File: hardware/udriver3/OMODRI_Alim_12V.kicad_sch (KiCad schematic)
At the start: 13 parts, among them U15 MP4572GQB

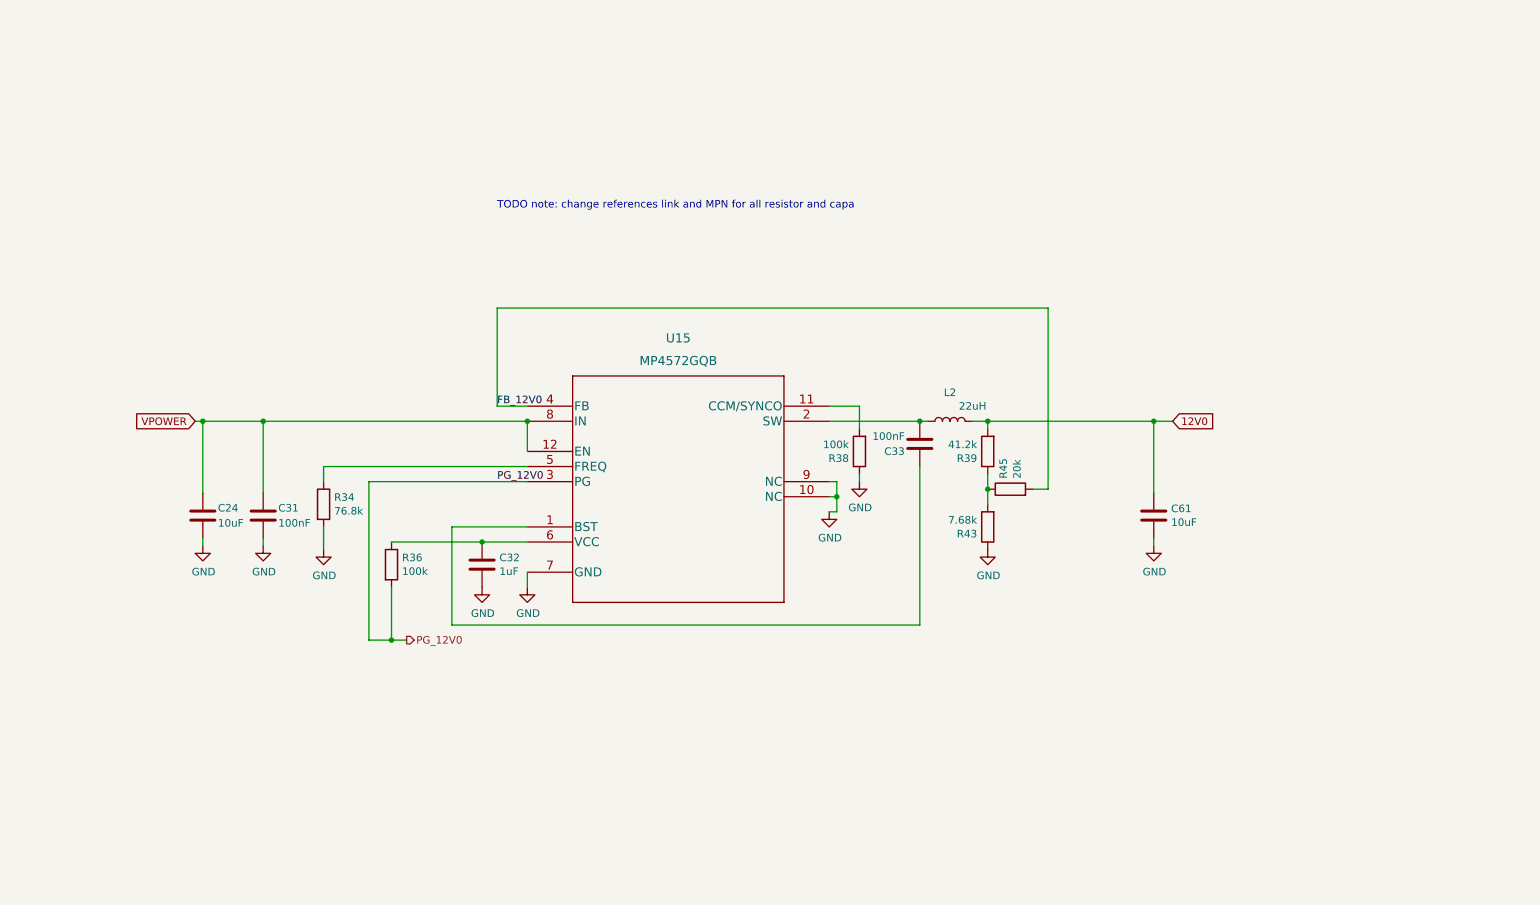
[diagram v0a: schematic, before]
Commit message: Schematics update. 12V0 and 5V0 power supplies not finished yet. RS485 added but not connected to F28388 mcu.
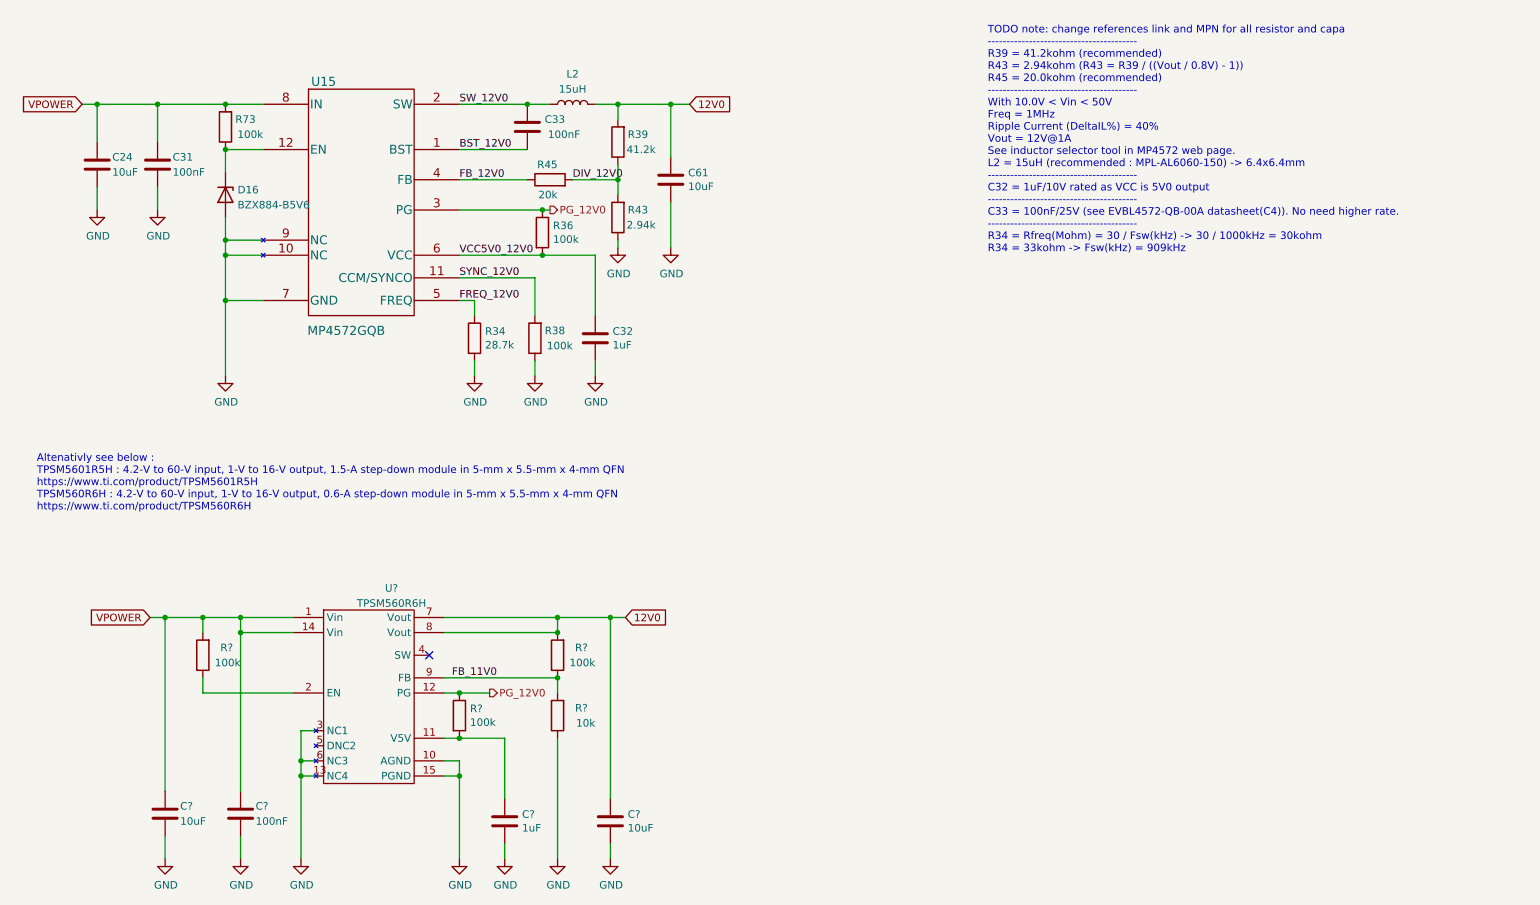
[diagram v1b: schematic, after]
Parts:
- added C?: 100nF, Capacitor_SMD:C_0603_1608Metric, symbol Device:C
- added C?: 10uF, Capacitor_SMD:C_1210_3225Metric, symbol Device:C
- added C?: 10uF, Capacitor_SMD:C_0603_1608Metric, symbol Device:C
- added C?: 1uF, Capacitor_SMD:C_0201_0603Metric, symbol Device:C
- added D16: BZX884-B5V6, udriver3:DFN1006-2, symbol Device:D_Zener
- added R73, R?: 100k, Resistor_SMD:R_0402_1005Metric, symbol Device:R
- added R? (x2): 100k, Resistor_SMD:R_0201_0603Metric, symbol Device:R
- added R?: 10k, Resistor_SMD:R_0201_0603Metric, symbol Device:R
- added U?: TPSM560R6H, symbol omodri_lib:TPSM560R6H
- C33: footprint Capacitor_SMD:C_0603_1608Metric -> Capacitor_SMD:C_0201_0603Metric; DigiKey 490-3285-1-ND -> 490-14571-1-ND; Farnell 1828921 -> 3790414; Mouser 81-GRM188R72A104KA35 -> 81-GRM033R61E104KE4J; Part No GRM188R72A104KA35D -> GRM033R61E104KE14J; RS (none) -> 185-2066; Rated Voltage 100V -> 25V
- C61: DigiKey 490-10475-1-ND -> 490-7202-2-ND; Farnell 2456110 -> 2695906; Mouser 81-GRM188R61A106ME9D -> 81-GRM188R61E106MA3D; Part No GRM188R61A106ME69D -> GRM188R61E106MA73D; RS 113-8702 -> 815-1377; Rated Voltage 10V -> 25V
- L2: value 22uH -> 15uH
- R34: value 76.8k -> 28.7k
- R43: value 7.68k -> 2.94k
- U15: footprint udriver3:MP4572GQB -> udriver3:QFN-12_2.5x3mm_P0.5mm_MPS; DigiKey (none) -> 1589-MP4572GQB-PTR-ND; Farnell (none) -> 3935113; Mouser (none) -> 946-MP4572GQB-P; Part No (none) -> MP4572GQB-P
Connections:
- net 12V0: now also C?.1, R?.2, U?.7 (Vout), U?.8 (Vout)
- net FB_12V0: now also R45.1; no longer R45.2
- net GND: now also C?.2, C?.2, C?.2, C?.2, D16.2 (A), R?.1, U?.10 (AGND), U?.13 (NC4), U?.15 (PGND), U?.3 (NC1), U?.6 (NC3)
- net PG_12V0: now also R36.1, R?.1, U?.12 (PG); no longer R36.2
- net VPOWER: now also C?.1, C?.1, R73.2, R?.2, U?.1 (Vin), U?.14 (Vin); no longer U15.12 (EN)
- net BST_12V0: now reaches C33.1, U15.1 (BST)
- net SYNC_12V0: now reaches R38.2, U15.11 (CCM/SYNCO)
- net SW_12V0: now reaches C33.2, L2.1, U15.2 (SW)
- net FREQ_12V0: now reaches R34.1, U15.5 (FREQ)
- net VCC5V0_12V0: now reaches C32.1, U15.6 (VCC)
- net VCC5V0_12V0: now also R36.2; no longer R36.1
- net DIV_12V0: now reaches R39.1, R43.2
- net DIV_12V0: now also R45.2; no longer R45.1
- new net: D16.1 (K), R73.1, U15.12 (EN)
- new net: C?.1, R?.2, U?.11 (V5V)
- new net: R?.1, U?.2 (EN)
- new net FB_11V0: R?.1, R?.2, U?.9 (FB)
- no-connect marks 0 -> 1
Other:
- note added: "Altenativly see below : TPSM5601R5H : 4.2-V to 60-V input, 1-V to 16-V output, 1.5-A step-down module in 5-mm x 5.5-mm x 4-mm QFN https://www.ti.com/product/TPSM5601R5H TPSM560R6H : 4.2-V to 60-V input, 1-V to 16-V output, 0.6-A step-down module in 5-mm x 5.5-mm x 4-mm QFN https://www.ti.com/product/TPSM560R6H"
- note added: "TODO note: change references link and MPN for all resistor and capa ---------------------------------------- R39 = 41.2kohm (recommended) R43 = 2.94kohm (R43 = R39 / ((Vout / 0.8V) - 1)) R45 = 20.0kohm (recommended) ---------------------------------------- With 10.0V < Vin < 50V Freq = 1MHz Ripple Current (DeltaIL%) = 40% Vout = 12V@1A See inductor selector tool in MP4572 web page. L2 = 15uH (rec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"
- note removed: "TODO note: change references link and MPN for all resistor and capa"
- company: (none) -> LAAS/CNRS
- title: (none) -> Open MOtor DRiver Initiative (OMODRI)
- moved on the sheet: C24, C31, C32, C33, C61, L2, R34, R36, R39, R43, R45

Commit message: Temporary version of udrive3 v2.0. - In schematic there are 2 solutions for DC/DC buck converter. - PCB routing is not finished yet.
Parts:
- removed R?: 100k, Resistor_SMD:R_0402_1005Metric, symbol Device:R
- R53: renamed from R?; DigiKey (none) -> P122655CT-ND; Farnell (none) -> 2302389; Mouser (none) -> 667-ERJ-1GNF1003C; Part No (none) -> ERJ-1GNF1003C; RS (none) -> 179-7130; Rated Voltage (none) -> Resistor_SMD:R_0201_0603Metric
- R59: renamed from R?; DigiKey (none) -> P122414CT-ND; Farnell (none) -> 2302362; Mouser (none) -> 667-ERJ-1GNF1002C; Part No (none) -> ERJ-1GNF1002C; RS (none) -> 176-3597
- U16: renamed from U?; footprint (none) -> udriver3:B3QFN_15; DigiKey (none) -> 296-TPSM560R6HRDARTR-ND; Mouser (none) -> 595-TPSM560R6HRDAR; Part No (none) -> TPSM560R6HRDAR
- gave numbers to parts that had none: 5
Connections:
- net 12V0: no longer C89.1, R53.2, U16.7 (Vout), U16.8 (Vout)
- net PG_12V0: no longer R57.1, U16.12 (PG)
- net VPOWER: now also U16.2 (EN)
- net EN_12V0: now reaches D16.1 (K), R73.1, U15.12 (EN)
- new net 12V0_1: C89.1, R53.2, U16.7 (Vout), U16.8 (Vout)
- new net PG_12V0_1: R57.1, U16.12 (PG)
- no-connect marks 1 -> 0

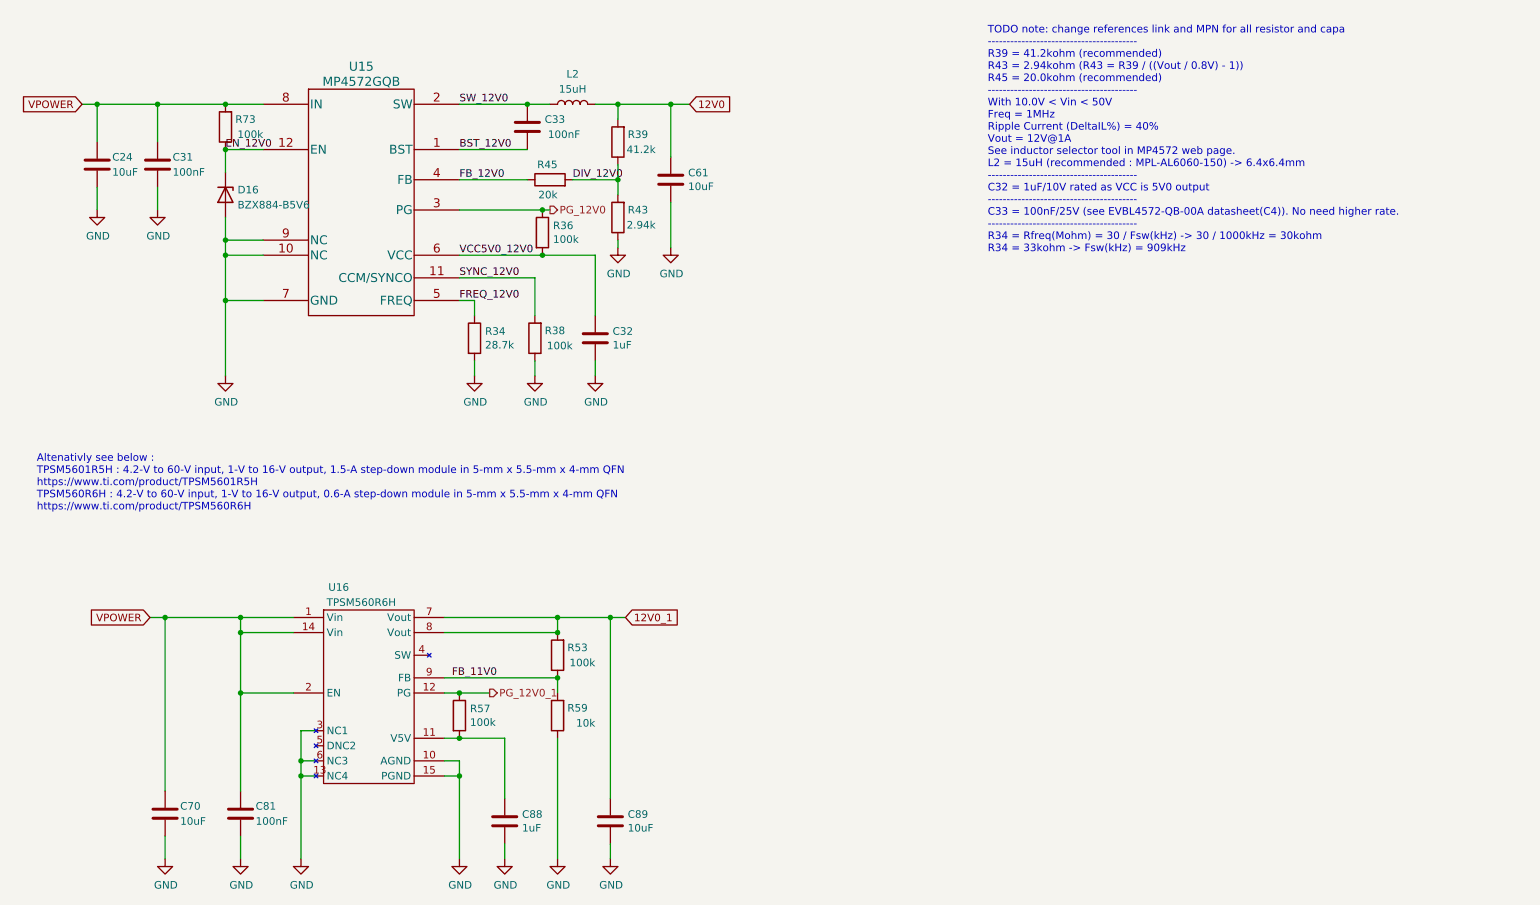
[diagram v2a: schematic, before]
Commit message: Some routing updates.
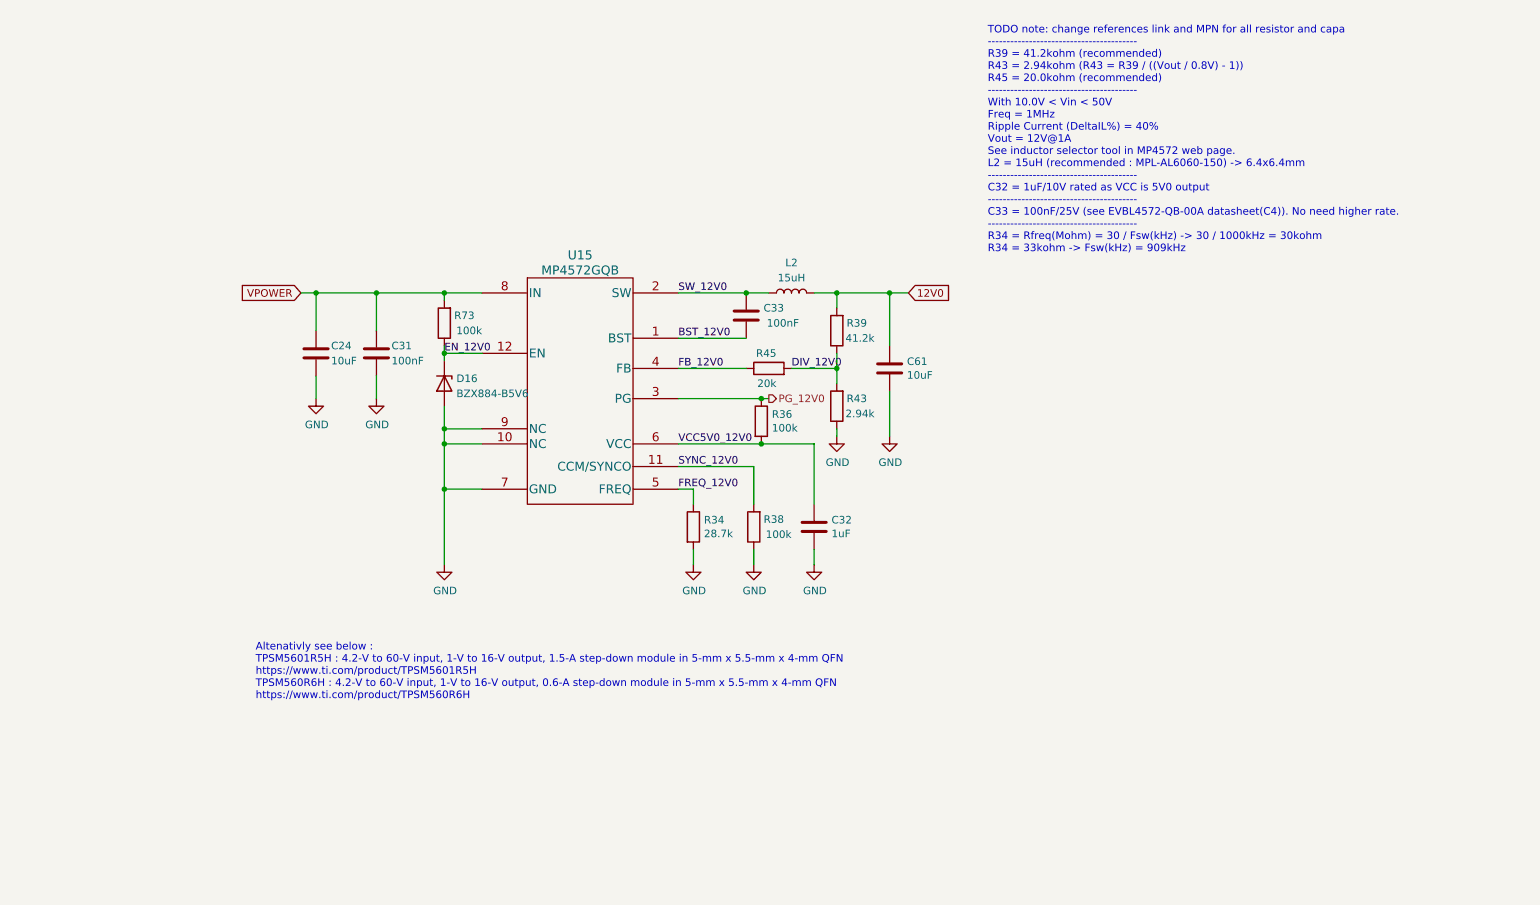
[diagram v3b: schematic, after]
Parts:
- removed C70: 10uF, Capacitor_SMD:C_1210_3225Metric, symbol Device:C
- removed C81: 100nF, Capacitor_SMD:C_0603_1608Metric, symbol Device:C
- removed C88: 1uF, Capacitor_SMD:C_0201_0603Metric, symbol Device:C
- removed C89: 10uF, Capacitor_SMD:C_0603_1608Metric, symbol Device:C
- removed R53, R57: 100k, Resistor_SMD:R_0201_0603Metric, symbol Device:R
- removed R59: 10k, Resistor_SMD:R_0201_0603Metric, symbol Device:R
- removed U16: TPSM560R6H, udriver3:B3QFN_15, symbol omodri_lib:TPSM560R6H
- R34: DigiKey (none) -> P122902TR-ND; Farnell (none) -> 3335257; Mouser (none) -> 667-ERJ-1GNF2872C; Part No (none) -> ERJ-1GNF2872C
- R39: DigiKey (none) -> P122998TR-ND; Farnell (none) -> 3302949; Mouser (none) -> 667-ERJ-1GNF4122C; Part No (none) -> ERJ-1GNF4122C
- R43: DigiKey (none) -> P122907TR-ND; Farnell (none) -> 3335262; Mouser (none) -> 667-ERJ-1GNF2941C; Part No (none) -> ERJ-1GNF2941C
- R45: DigiKey (none) -> P122813TR-ND; Farnell (none) -> 2396915; Mouser (none) -> 667-ERJ-1GNF2002C; Part No (none) -> ERJ-1GNF2002C
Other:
- moved on the sheet: C24, C31, C32, C33, C61, D16, L2, R34, R36, R38, R39, R43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

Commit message: PCB routing update.
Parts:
- added C70: 10uF, Capacitor_SMD:C_1210_3225Metric, symbol Device:C
- added C81: 100nF, Capacitor_SMD:C_0603_1608Metric, symbol Device:C
- added C88: 22uF, Capacitor_SMD:C_0805_2012Metric, symbol Device:C
- added R66: 100k, Resistor_SMD:R_0201_0603Metric, symbol Device:R
- added R67: 9.09k, Resistor_SMD:R_0201_0603Metric, symbol Device:R
- added U9: TPSM560R6H, udriver3:B3QFN_15, symbol omodri_lib:TPSM560R6H
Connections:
- net GND: now also C70.2, C81.2, C88.2, R67.1, U9.10 (AGND), U9.15 (PGND)
- net VPOWER: now also C70.1, C81.1, U9.1 (Vin), U9.14 (Vin), U9.2 (EN)
- new net 12V1: C88.1, R66.1, U9.7 (Vout), U9.8 (Vout)
- new net FB_12V1: R66.2, R67.2, U9.9 (FB)
- no-connect marks 0 -> 2
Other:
- moved on the sheet: C24, C31, C32, C33, C61, D16, L2, R34, R36, R38, R39, R43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
